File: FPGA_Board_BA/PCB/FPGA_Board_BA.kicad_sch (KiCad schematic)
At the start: 3 parts

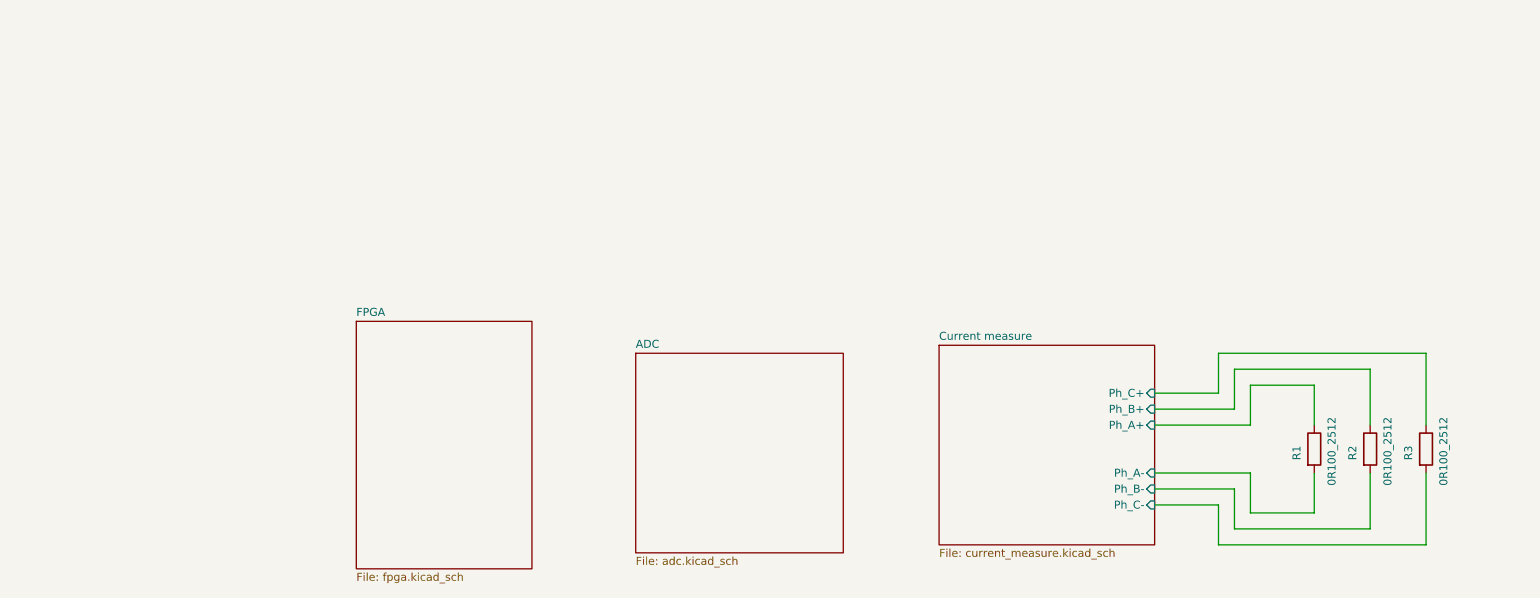
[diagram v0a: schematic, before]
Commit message: adding DCCD
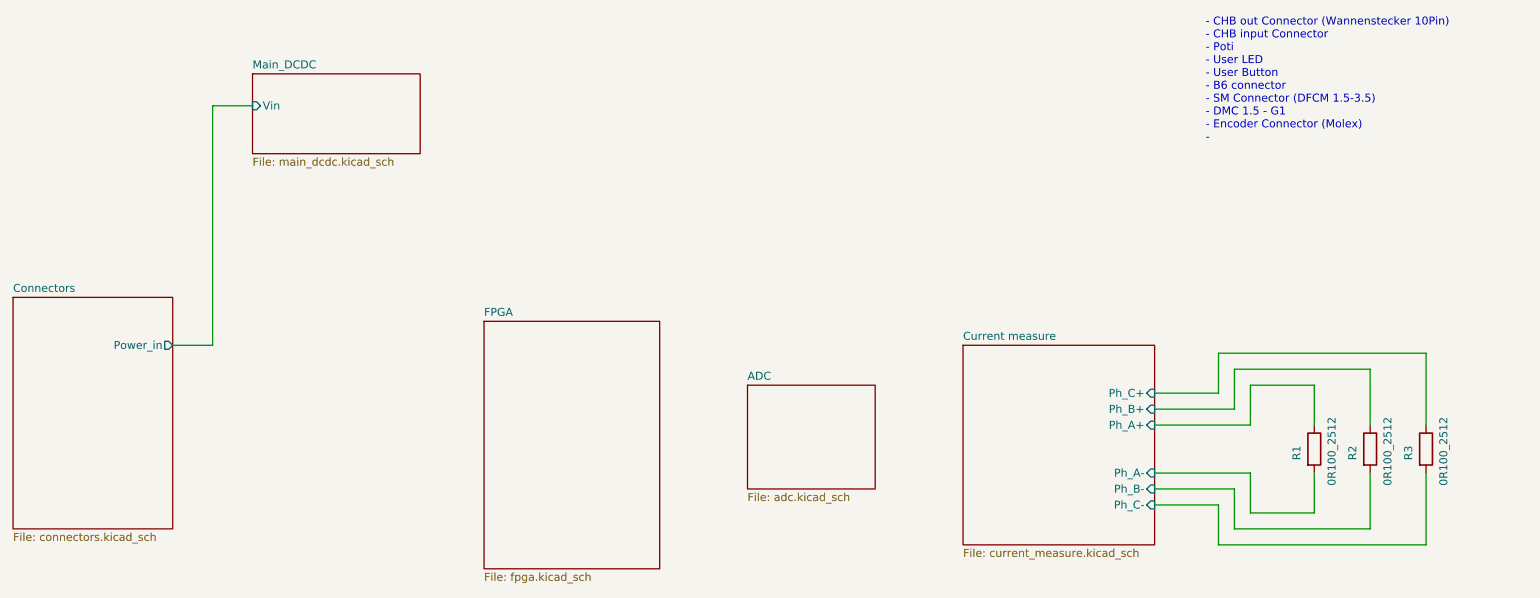
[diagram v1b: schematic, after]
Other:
- added sheet Connectors (connectors.kicad_sch)
- added sheet Main_DCDC (main_dcdc.kicad_sch)
- note added: "- CHB out Connector (Wannenstecker 10Pin) - CHB input Connector - Poti - User LED - User Button - B6 connector - SM Connector (DFCM 1.5-3.5) - DMC 1.5 - G1 - Encoder Connector (Molex) -"
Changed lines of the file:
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@@
 	(generator_version "9.0")
 	(paper "A4")
+	(text "- CHB out Connector (Wannenstecker 10Pin)\n- CHB input Connector\n- Poti\n- User LED\n- User Button\n- B6 connector\n- SM Connector (DFCM 1.5-3.5)\n- DMC 1.5 - G1\n- Encoder Connector (Molex)\n- "
+		(exclude_from_sim no)
+		(at 220.218 34.036 0)
+		(effects
+			(font
+				(size 1.27 1.27)
+			)
+			(justify left)
+		)
+	)
 	(wire
 		(pts
@@
 	(wire
 		(pts
+			(xy 62.23 38.1) (xy 68.58 38.1)
+		)
+		(stroke
+			(width 0)
+			(type default)
+		)
+	)
+	(wire
+		(pts
 			(xy 222.25 77.47) (xy 255.27 77.47)
 		)
@@
 	(wire
 		(pts
+			(xy 62.23 76.2) (xy 62.23 38.1)
+		)
+		(stroke
+			(width 0)
+			(type default)
+		)
+	)
+	(wire
+		(pts
 			(xy 212.09 99.06) (xy 224.79 99.06)
 		)
@@
 		(pts
 			(xy 224.79 99.06) (xy 224.79 105.41)
+		)
+		(stroke
+			(width 0)
+			(type default)
+		)
+	)
+	(wire
+		(pts
+			(xy 55.88 76.2) (xy 62.23 76.2)
 		)
 		(stroke
@@
 	)
 	(sheet
-		(at 177.8 76.2)
-		(size 34.29 31.75)
+		(at 30.48 68.58)
+		(size 25.4 36.83)
 		(exclude_from_sim no)
 		(in_bom yes)
@@
 			(color 0 0 0 0.0000)
 		)
+		(property "Sheetname" "Connectors"
+			(at 30.48 67.8684 0)
+			(effects
+				(font
+					(size 1.27 1.27)
+				)
+				(justify left bottom)
+			)
+		)
+		(property "Sheetfile" "connectors.kicad_sch"
+			(at 30.48 105.9946 0)
+			(effects
+				(font
+					(size 1.27 1.27)
+				)
+				(justify left top)
+			)
+		)
+		(pin "Power_in" output
+			(at 55.88 76.2 0)
+			(effects
+				(font
+					(size 1.27 1.27)
+				)
+				(justify right)
+			)
+		)
+		(instances
+			(project "FPGA_Board_BA"
+				(path "/fd7503bc-e7fc-4766-b224-3d1c3d7de5ff"
+					(page "6")
+				)
+			)
+		)
+	)
+	(sheet
+		(at 181.61 76.2)
+		(size 30.48 31.75)
+		(exclude_from_sim no)
+		(in_bom yes)
+		(on_board yes)
+		(dnp no)
+		(fields_autoplaced yes)
+		(stroke
+			(width 0.1524)
+			(type solid)
+		)
+		(fill
+			(color 0 0 0 0.0000)
+		)
 		(property "Sheetname" "Current measure"
-			(at 177.8 75.4884 0)
+			(at 181.61 75.4884 0)
 			(effects
 				(font
@@
 		)
 		(property "Sheetfile" "current_measure.kicad_sch"
-			(at 177.8 108.5346 0)
+			(at 181.61 108.5346 0)
 			(effects
 				(font
@@
 	)
 	(sheet
-		(at 85.09 72.39)
+		(at 105.41 72.39)
 		(size 27.94 39.37)
 		(exclude_from_sim no)
@@
 		)
 		(property "Sheetname" "FPGA"
-			(at 85.09 71.6784 0)
+			(at 105.41 71.6784 0)
 			(effects
 				(font
@@
 		)
 		(property "Sheetfile" "fpga.kicad_sch"
-			(at 85.09 112.3446 0)
+			(at 105.41 112.3446 0)
 			(effects
 				(font
@@
 	)
 	(sheet
-		(at 129.54 77.47)
-		(size 33.02 31.75)
+		(at 147.32 82.55)
+		(size 20.32 16.51)
 		(exclude_from_sim no)
 		(in_bom yes)
@@
 		)
 		(property "Sheetname" "ADC"
-			(at 129.54 76.7584 0)
+			(at 147.32 81.8384 0)
 			(effects
 				(font
@@
 		)
 		(property "Sheetfile" "adc.kicad_sch"
-			(at 129.54 109.8046 0)
+			(at 147.32 99.6446 0)
 			(effects
 				(font
@@
 				)
 			)
+		)
+	)
+	(sheet
+		(at 68.58 33.02)
+		(size 26.67 12.7)
+		(exclude_from_sim no)
+		(in_bom yes)
+		(on_board yes)
+		(dnp no)
+		(fields_autoplaced yes)
+		(stroke
+			(width 0.1524)
+			(type solid)
+		)
+		(fill
+			(color 0 0 0 0.0000)
+		)
+		(property "Sheetname" "Main_DCDC"
+			(at 68.58 32.3084 0)
+			(effects
+				(font
+					(size 1.27 1.27)
+				)
+				(justify left bottom)
+			)
+		)
+		(property "Sheetfile" "main_dcdc.kicad_sch"
+			(at 68.58 46.3046 0)
+			(effects
+				(font
+					(size 1.27 1.27)
+				)
+				(justify left top)
+			)
+		)
+		(pin "Vin" input
+			(at 68.58 38.1 180)
+			(effects
+				(font
+					(size 1.27 1.27)
+				)
+				(justify left)
+			)
+		)
+		(instances
+			(project "FPGA_Board_BA"
+				(path "/fd7503bc-e7fc-4766-b224-3d1c3d7de5ff"
+					(page "5")
+				)
+			)

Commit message: some work on the schematics
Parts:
- added J101: Box_Header_2x05_THT, Connector_IDC:IDC-Header_2x05_P2.54mm_Vertical, symbol MYLIB_Misc:Box_Header_10pin
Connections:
- net Current measure/Ph_A- renamed CHB to 3Ph/Ph_A1_out
- net Current measure/Ph_B- renamed CHB to 3Ph/Ph_B1_out
- net Current measure/Ph_C- renamed CHB to 3Ph/Ph_C1_out
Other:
- added sheet CHB to 3Ph (chb_to_3ph.kicad_sch)
- added sheet Power from CHB (power_from_chb.kicad_sch)
- added sheet User Interaction (user_interaction.kicad_sch)
- note added: "[X] CHB input Connector (Wannenstecker 10Pin) [X] CHB output Connector - Poti - User LED - User Button - B6 connector [X] SM Connector (DFCM 1.5-3.5) [X] DMC 1.5 - G1 - Encoder Connector (Molex)"
- note removed: "- CHB out Connector (Wannenstecker 10Pin) - CHB input Connector - Poti - User LED - User Button - B6 connector - SM Connector (DFCM 1.5-3.5) - DMC 1.5 - G1 - Encoder Connector (Molex) -"
- moved on the sheet: R1, R2, R3

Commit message: some stuff
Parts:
- removed J101: Box_Header_2x05_THT, Connector_IDC:IDC-Header_2x05_P2.54mm_Vertical, symbol MYLIB_Misc:Box_Header_10pin
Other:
- added sheet CHB Communication (chb_com.kicad_sch)
- added sheet Encoder (encoder.kicad_sch)
- note added: "[X] CHB input Connector (Wannenstecker 10Pin) [X] CHB output Connector - Poti [X] User LED [X] User Button - B6 connector [X] SM Connector (DFCM 1.5-3.5) [X] DMC 1.5 - G1 [X] Encoder Connector (Molex) [X] Phoenix Connector statt BoxHeaders - Power Buffer for clean 5V der FPGA"
- note removed: "[X] CHB input Connector (Wannenstecker 10Pin) [X] CHB output Connector - Poti - User LED - User Button - B6 connector [X] SM Connector (DFCM 1.5-3.5) [X] DMC 1.5 - G1 - Encoder Connector (Molex)"
- moved on the sheet: R1, R2, R3

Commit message: schematic almost ready
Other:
- added sheet Analog Voltage (analog_voltage.kicad_sch)
- added sheet TI-B6 (ti_b6.kicad_sch)
- sheet ADC ports: added CLK_IN, CLK_OUT, I_A, I_B, I_C, SDO1, SDO2, SDO3, SDO4, SDO5, SDO6, SDO7, SDO8, V_A, V_B, V_C, V_DC, ~{CNV}; removed none
- sheet CHB Communication ports: added Ph_A_En, Ph_A_Err, Ph_A_Rx, Ph_B_En, Ph_B_Err, Ph_B_Rx, Ph_C_En, Ph_C_Err, Ph_C_Rx, Ph_C_Tx1, Ph_C_Tx10, Ph_C_Tx11, Ph_C_Tx12, Ph_C_Tx2, Ph_C_Tx3, Ph_C_Tx4, Ph_C_Tx5, Ph_C_Tx6, Ph_C_Tx7, Ph_C_Tx8, Ph_C_Tx9, Ph_D_En, Ph_D_Err, Ph_D_Rx, Ph_D_Tx1, Ph_D_Tx10, Ph_D_Tx11, Ph_D_Tx12, Ph_D_Tx2, Ph_D_Tx3, Ph_D_Tx4, Ph_D_Tx5, Ph_D_Tx6, Ph_D_Tx7, Ph_D_Tx8, Ph_D_Tx9; removed none
- sheet Current measure ports: added PHA_OUTN, PHA_OUTP, PHB_OUTN, PHB_OUTP, PHC_OUTN, PHC_OUTP; removed none
- sheet FPGA ports: added B6_En, CLK_IN, CLK_OUT, ENC_A_in, ENC_B_in, ENC_I_in, OT, PWM_AH, PWM_AL, PWM_BH, PWM_BL, PWM_CH, PWM_CL, Ph_A_En, Ph_A_Err, Ph_A_Rx, Ph_A_Tx1, Ph_A_Tx10, Ph_A_Tx11, Ph_A_Tx12, Ph_A_Tx2, Ph_A_Tx3, Ph_A_Tx4, Ph_A_Tx5, Ph_A_Tx6, Ph_A_Tx7, Ph_A_Tx8, Ph_A_Tx9, Ph_B_En, Ph_B_Err, Ph_B_Rx, Ph_B_Tx1, Ph_B_Tx10, Ph_B_Tx11, Ph_B_Tx12, Ph_B_Tx2, Ph_B_Tx3, Ph_B_Tx4, Ph_B_Tx5, Ph_B_Tx6, Ph_B_Tx7, Ph_B_Tx8, Ph_B_Tx9, Ph_C_En, Ph_C_Err, Ph_C_Rx, Ph_C_Tx1, Ph_C_Tx10, Ph_C_Tx11, Ph_C_Tx12, Ph_C_Tx2, Ph_C_Tx3, Ph_C_Tx4, Ph_C_Tx5, Ph_C_Tx6, Ph_C_Tx7, Ph_C_Tx8, Ph_C_Tx9, Ph_D_En, Ph_D_Err, Ph_D_Rx, Ph_D_Tx1, Ph_D_Tx10, Ph_D_Tx11, Ph_D_Tx12, Ph_D_Tx2, Ph_D_Tx3, Ph_D_Tx4, Ph_D_Tx5, Ph_D_Tx6, Ph_D_Tx7, Ph_D_Tx8, Ph_D_Tx9, SDO1, SDO2, SDO3, SDO4, SDO5, SDO6, SDO7, SDO8, ~{CNV}; removed none
- sheet Main_DCDC ports: added Vout; removed none
- note added: "[X] CHB input Connector (Wannenstecker 10Pin) [X] CHB output Connector - Poti [X] User LED [X] User Button [X] B6 connector [X] SM Connector (DFCM 1.5-3.5) [X] DMC 1.5 - G1 [X] Encoder Connector (Molex) [X] Phoenix Connector statt BoxHeaders [X] Power Buffer for clean 5V for Analog [X] FPGA cleanup - DCDC for Differential-amplifier - ADC power supply (U < 3V) - Breakout for all unused pins [X] Rx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"
- note removed: "[X] CHB input Connector (Wannenstecker 10Pin) [X] CHB output Connector - Poti [X] User LED [X] User Button - B6 connector [X] SM Connector (DFCM 1.5-3.5) [X] DMC 1.5 - G1 [X] Encoder Connector (Molex) [X] Phoenix Connector statt BoxHeaders - Power Buffer for clean 5V der FPGA"
- moved on the sheet: R1, R2, R3

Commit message: schematic almost ready pt2
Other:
- sheet FPGA ports: added Button1, Button2, LED1, LED2, Poti; removed none
- note added: "[X] CHB input Connector (Wannenstecker 10Pin) [X] CHB output Connector [X] Poti [X] User LED [X] User Button [X] B6 connector [X] SM Connector (DFCM 1.5-3.5) [X] DMC 1.5 - G1 [X] Encoder Connector (Molex) [X] Phoenix Connector statt BoxHeaders [X] Power Buffer for clean 5V for Analog [X] FPGA cleanup - DCDC for Differential-amplifier - ADC power supply (1.8V ... 2.5V) - Breakout for all unused pi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"
- note removed: "[X] CHB input Connector (Wannenstecker 10Pin) [X] CHB output Connector - Poti [X] User LED [X] User Button [X] B6 connector [X] SM Connector (DFCM 1.5-3.5) [X] DMC 1.5 - G1 [X] Encoder Connector (Molex) [X] Phoenix Connector statt BoxHeaders [X] Power Buffer for clean 5V for Analog [X] FPGA cleanup - DCDC for Differential-amplifier - ADC power supply (U < 3V) - Breakout for all unused pins [X] Rx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"
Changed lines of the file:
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@@
 	(generator_version "9.0")
 	(paper "A3")
-	(text "[X] CHB input Connector (Wannenstecker 10Pin)\n[X] CHB output Connector\n- Poti\n[X] User LED\n[X] User Button\n[X] B6 connector\n[X] SM Connector (DFCM 1.5-3.5)\n[X] DMC 1.5 - G1\n[X] Encoder Connector (Molex)\n[X] Phoenix Connector statt BoxHeaders\n[X] Power Buffer for clean 5V for Analog\n[X] FPGA cleanup\n- DCDC for Differential-amplifier\n- ADC power supply (U < 3V)\n- Breakout for all unused pins\n[X] Rx, En, Err pins"
+	(text "[X] CHB input Connector (Wannenstecker 10Pin)\n[X] CHB output Connector\n[X] Poti\n[X] User LED\n[X] User Button\n[X] B6 connector\n[X] SM Connector (DFCM 1.5-3.5)\n[X] DMC 1.5 - G1\n[X] Encoder Connector (Molex)\n[X] Phoenix Connector statt BoxHeaders\n[X] Power Buffer for clean 5V for Analog\n[X] FPGA cleanup\n- DCDC for Differential-amplifier\n- ADC power supply (1.8V ... 2.5V)\n- Breakout for all unused pins\n[X] Single ESD Diodes for unused pins\n- ESD Diode Array for unused pins\n[X] Rx, En, Err pins\n[X] Power LEDs"
 		(exclude_from_sim no)
 		(at 28.702 98.806 0)
@@
 	(wire
 		(pts
+			(xy 109.22 62.23) (xy 156.21 62.23)
+		)
+		(stroke
+			(width 0)
+			(type default)
+		)
+	)
+	(wire
+		(pts
 			(xy 198.12 139.7) (xy 223.52 139.7)
 		)
@@
 	(wire
 		(pts
+			(xy 109.22 67.31) (xy 156.21 67.31)
+		)
+		(stroke
+			(width 0)
+			(type default)
+		)
+	)
+	(wire
+		(pts
 			(xy 198.12 90.17) (xy 226.06 90.17)
 		)
@@
 	(wire
 		(pts
+			(xy 109.22 72.39) (xy 156.21 72.39)
+		)
+		(stroke
+			(width 0)
+			(type default)
+		)
+	)
+	(wire
+		(pts
 			(xy 317.5 99.06) (xy 353.06 99.06)
 		)
@@
 	(wire
 		(pts
+			(xy 109.22 64.77) (xy 156.21 64.77)
+		)
+		(stroke
+			(width 0)
+			(type default)
+		)
+	)
+	(wire
+		(pts
 			(xy 342.9 96.52) (xy 342.9 107.95)
 		)
@@
 		(pts
 			(xy 198.12 92.71) (xy 226.06 92.71)
+		)
+		(stroke
+			(width 0)
+			(type default)
+		)
+	)
+	(wire
+		(pts
+			(xy 109.22 69.85) (xy 156.21 69.85)
 		)
 		(stroke
@@
 	)
 	(sheet
-		(at 85.09 116.84)
-		(size 25.4 161.29)
+		(at 76.2 116.84)
+		(size 34.29 161.29)
 		(exclude_from_sim no)
 		(in_bom yes)
@@
 		)
 		(property "Sheetname" "CHB Communication"
-			(at 84.836 116.078 0)
+			(at 75.946 116.078 0)
 			(effects
 				(font
@@
 		)
 		(property "Sheetfile" "chb_com.kicad_sch"
-			(at 85.09 278.892 0)
+			(at 76.2 278.892 0)
 			(effects
 				(font
@@
 			)
 		)
+		(pin "Button1" input
+			(at 156.21 62.23 180)
+			(effects
+				(font
+					(size 1.27 1.27)
+				)
+				(justify left)
+			)
+		)
+		(pin "Button2" input
+			(at 156.21 64.77 180)
+			(effects
+				(font
+					(size 1.27 1.27)
+				)
+				(justify left)
+			)
+		)
+		(pin "LED1" output
+			(at 156.21 67.31 180)
+			(effects
+				(font
+					(size 1.27 1.27)
+				)
+				(justify left)
+			)
+		)
+		(pin "LED2" output
+			(at 156.21 69.85 180)
+			(effects
+				(font
+					(size 1.27 1.27)
+				)
+				(justify left)
+			)
+		)
+		(pin "Poti" input
+			(at 156.21 72.39 180)
+			(effects
+				(font
+					(size 1.27 1.27)
+				)
+				(justify left)
+			)
+		)

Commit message: Besprechung mit Leo
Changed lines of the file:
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@@
 	(generator_version "9.0")
 	(paper "A3")
-	(text "[X] CHB input Connector (Wannenstecker 10Pin)\n[X] CHB output Connector\n[X] Poti\n[X] User LED\n[X] User Button\n[X] B6 connector\n[X] SM Connector (DFCM 1.5-3.5)\n[X] DMC 1.5 - G1\n[X] Encoder Connector (Molex)\n[X] Phoenix Connector statt BoxHeaders\n[X] Power Buffer for clean 5V for Analog\n[X] FPGA cleanup\n- DCDC for Differential-amplifier\n- ADC power supply (1.8V ... 2.5V)\n- Breakout for all unused pins\n[X] Single ESD Diodes for unused pins\n- ESD Diode Array for unused pins\n[X] Rx, En, Err pins\n[X] Power LEDs"
+	(text "[X] CHB input Connector (Wannenstecker 10Pin)\n[X] CHB output Connector\n[X] Poti\n[X] User LED\n[X] User Button\n[X] B6 connector\n[X] SM Connector (DFCM 1.5-3.5)\n[X] DMC 1.5 - G1\n[X] Encoder Connector (Molex)\n[X] Phoenix Connector statt BoxHeaders\n[X] Power Buffer for clean 5V for Analog\n[X] FPGA cleanup\n- DCDC for Differential-amplifier\n- ADC power supply (1.8V ... 2.5V)\n- Breakout for all unused pins\n[X] Single ESD Diodes for unused pins\n- ESD Diode Array for unused pins\n[X] Rx, En, Err pins\n[X] Power LEDs\n- Add another ADC for B6\n- CHB Rx En Err -> 10 pin (wie base board)\n- Poti an Analog Input\n- ADC Datenbatt Recherche LVDS/CMOS ob 24pin + 2pins für comversion start frei sind\n- FPGA falsche pin namen an Hersteller + BA \n- Level shifter für Tx Rx und Fault pins (CHB -> FPGA)\n- Pullup Resistor für Tx der CHB und auch Rx\n- Latex dokumentation beginnen"
 		(exclude_from_sim no)
 		(at 28.702 98.806 0)

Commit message: some schematic changes + Misc
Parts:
- added R101: 0R100_2512, Resistor_SMD:R_2512_6332Metric_Pad1.40x3.35mm_HandSolder, symbol MYLIB_R:0R100_2512
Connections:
- net CHB to 3Ph/Ph_D1_out: now also R101.2
- new net Current measure/Ph_D+: R101.1
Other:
- sheet ADC renamed ADC for B6
- added sheet ADC for Machine (adc_machine.kicad_sch)
- added sheet Voltage Measure (voltage_meas.kicad_sch)
- sheet Current measure ports: added PHD_OUTN, PHD_OUTP, Ph_D+, Ph_D-; removed none
- sheet FPGA ports: added CLK_IN_1, CLK_OUT_1, SDO1_1, SDO2_1, SDO3_1, SDO4_1, SDO5_1, SDO6_1, SDO7_1, SDO8_1, ~{CNV}_1; removed none
- note added: "- DCDC for Differential-amplifier - ADC power supply (1.8V ... 2.5V) - Breakout for all unused pins - ESD Diode Array for unused pins [X] Add another ADC for B6 - CHB Rx En Err -> 10 pin (wie base board) - Poti an Analog Input - ADC Datenbatt Recherche LVDS/CMOS ob 24pin + 2pins für comversion start frei sind - FPGA falsche pin namen an Hersteller + BA - Level shifter für Tx Rx und Fault pins (CH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"
- note removed: "[X] CHB input Connector (Wannenstecker 10Pin) [X] CHB output Connector [X] Poti [X] User LED [X] User Button [X] B6 connector [X] SM Connector (DFCM 1.5-3.5) [X] DMC 1.5 - G1 [X] Encoder Connector (Molex) [X] Phoenix Connector statt BoxHeaders [X] Power Buffer for clean 5V for Analog [X] FPGA cleanup - DCDC for Differential-amplifier - ADC power supply (1.8V ... 2.5V) - Breakout for all unused pi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"
